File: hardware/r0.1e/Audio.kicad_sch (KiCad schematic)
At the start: 84 parts, among them IC1 LM4861M, J1 Kenwood-2.5, J11 Radio_Opt, J12 Speaker, J4 CAT_TX, J5 Kenwood-3.5, J6 CAT_TX, J7 Radio, Q1 IRLML2060, Q2 BSS138, Q3 BSS138, U1 MAX9814, U6 MCP6002, U7 MCP6002

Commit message: Updated JLC fabrication files
Replaced reset button and BSS138 FETs
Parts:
- Q2, Q3: LCSC Part # C2912548 -> C400505
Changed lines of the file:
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@@
       (effects (font (size 1.27 1.27)) hide)
     )
-    (property "LCSC Part #" "C2912548" (at 153.67 185.42 0)
+    (property "LCSC Part #" "C400505" (at 153.67 185.42 0)
       (effects (font (size 1.27 1.27)) hide)
     )
@@
       (effects (font (size 1.27 1.27)) hide)
     )
-    (property "LCSC Part #" "C2912548" (at 137.16 158.75 0)
-      (effects (font (size 1.27 1.27)) hide)
-    )
+    (property "LCSC Part #" "C400505" (at 137.16 158.75 0)
+      (effects (font (size 1.27 1.27)) hide)
+    )

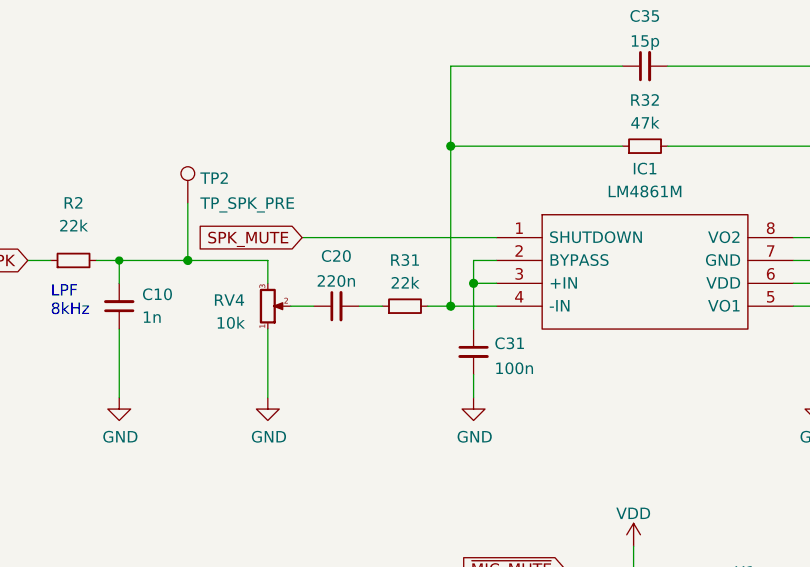
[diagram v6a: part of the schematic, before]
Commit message: Changed R31 to 1k8
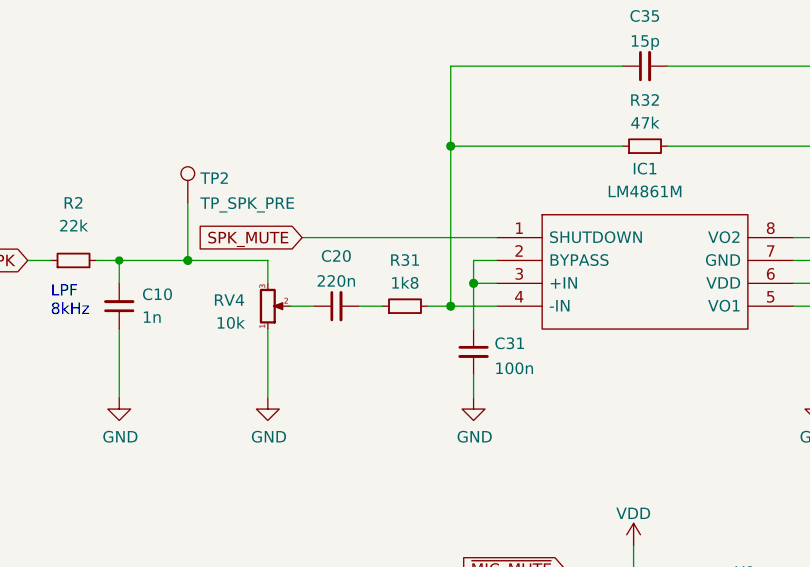
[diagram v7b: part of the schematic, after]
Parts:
- R31: value 22k -> 1k8; MPN Generic R/22k/0603 -> Generic R/1k8/0603
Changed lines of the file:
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@@
       (effects (font (size 1.27 1.27)))
     )
-    (property "Value" "22k" (at 67.31 44.45 90)
+    (property "Value" "1k8" (at 67.31 44.45 90)
       (effects (font (size 1.27 1.27)))
     )
@@
       (effects (font (size 1.524 1.524)))
     )
-    (property "MPN" "Generic R/22k/0603" (at 67.31 46.99 0)
+    (property "MPN" "Generic R/1k8/0603" (at 67.31 46.99 0)
       (effects (font (size 1.27 1.27)) hide)
     )
